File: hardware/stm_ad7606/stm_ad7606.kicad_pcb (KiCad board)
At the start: 2 copper layers, 40.6 x 55.6 mm, 28 parts, among them J1 Conn_01x02_Female, J2 USB_B_Micro, J4 AD7606 Interface, J5 SWD Conn, U1 STM32F103C8Tx, U2 AMS1117-3.3, Y1 8MHz

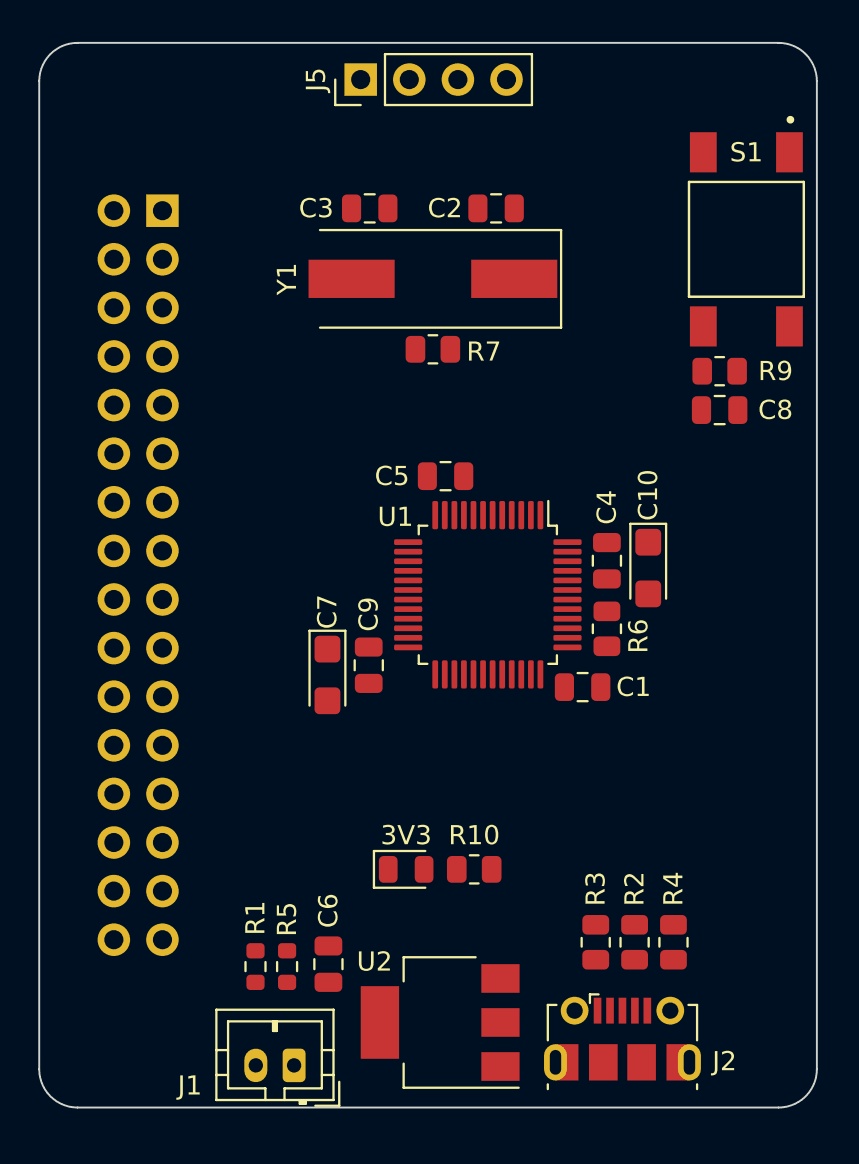
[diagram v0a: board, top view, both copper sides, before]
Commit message: feat[hw]: add interface connection MCU vs 7606
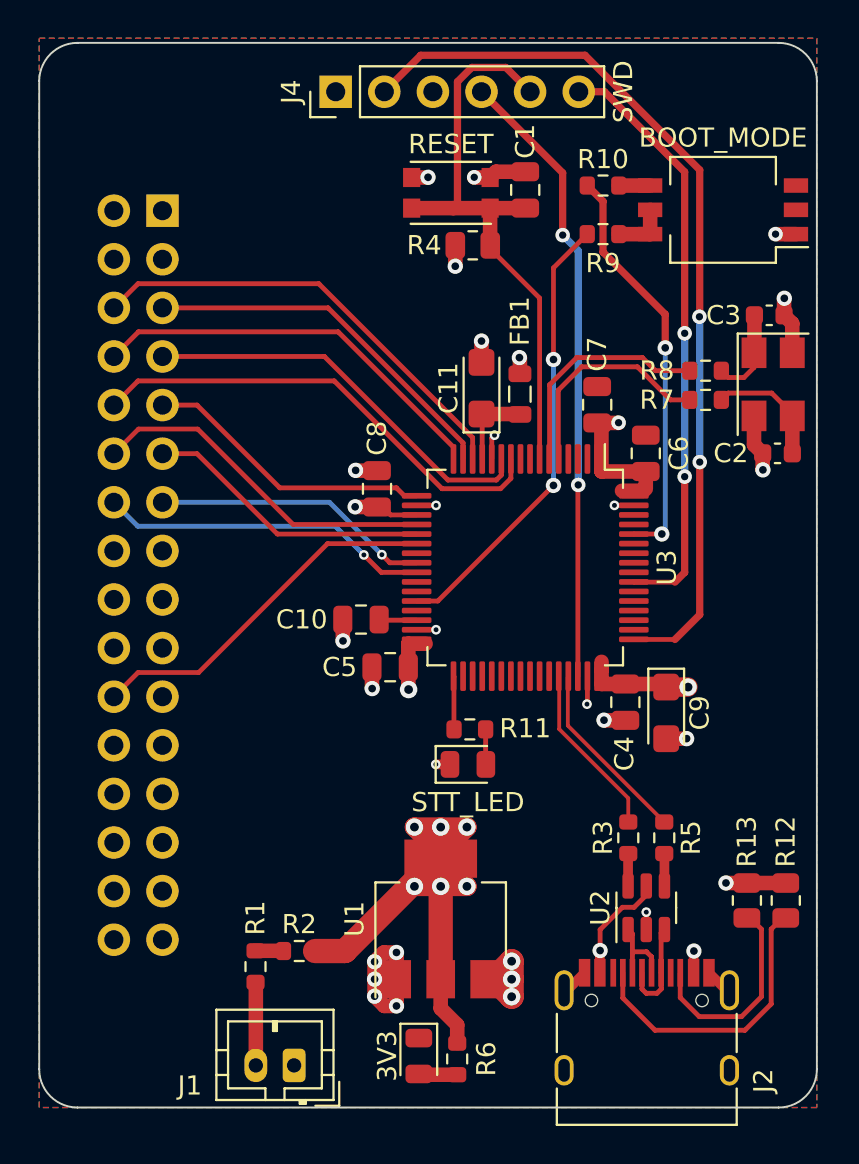
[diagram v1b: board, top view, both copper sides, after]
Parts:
- removed J5: SWD Conn, Connector_PinHeader_2.54mm:PinHeader_1x04_P2.54mm_Vertical
- removed the R2 at (150.2, 113.6)
- added C11: 10u, Capacitor_Tantalum_SMD:CP_EIA-3216-10_Kemet-I, F.Cu at (142.2, 84.6)
- added D2: STT_LED, LED_SMD:LED_0805_2012Metric, F.Cu at (141.5, 104.3)
- added FB1: 600R@100MHz, Inductor_SMD:L_0805_2012Metric, F.Cu at (144.2, 84.9)
- added J4: SWD, Connector_PinHeader_2.54mm:PinHeader_1x06_P2.54mm_Vertical, F.Cu at (134.5, 69.1)
- added R11: 2.49k, Resistor_SMD:R_0603_1608Metric, F.Cu at (141.6, 102.4)
- added R12: 5.1k, Resistor_SMD:R_0805_2012Metric, F.Cu at (158.1, 111.4)
- added R13: 5.1k, Resistor_SMD:R_0805_2012Metric, F.Cu at (156.0, 111.4)
- added R5: 22R, Resistor_SMD:R_0603_1608Metric, F.Cu at (151.7, 108.1)
- added R8: 220R, Resistor_SMD:R_0603_1608Metric, F.Cu at (153.9, 83.7)
- added SW1: BOOT_MODE, Button_Switch_SMD:SW_DIP_SPSTx03_Slide_KingTek_DSHP03TS_W7.62mm_P1.27mm, F.Cu at (154.8, 75.3)
- added U3: STM32F412RETx, Package_QFP:LQFP-64_10x10mm_P0.5mm, F.Cu at (144.5, 94.0)
- C1, C4, C5, C6, C8: value 100nF -> 100n
- C10, C7: value 10uF -> 100n; footprint Capacitor_Tantalum_SMD:CP_EIA-3216-10_Kemet-I -> Capacitor_SMD:C_0805_2012Metric
- C2, C3: value 22pF -> 22p; footprint Capacitor_SMD:C_0805_2012Metric -> Capacitor_SMD:C_0603_1608Metric
- C9: value 100nF -> 10u; footprint Capacitor_SMD:C_0805_2012Metric -> Capacitor_Tantalum_SMD:CP_EIA-3216-10_Kemet-I
- J2: value USB_B_Micro -> USB_C_Receptacle_USB2.0; footprint Connector_USB:USB_Micro-B_Molex-105017-0001 -> Connector_USB:USB_C_Receptacle_HRO_TYPE-C-31-M-12
- R10: value 1k -> 10k; footprint Resistor_SMD:R_0805_2012Metric -> Resistor_SMD:R_0603_1608Metric
- R3: value 20R -> 22R; footprint Resistor_SMD:R_0805_2012Metric -> Resistor_SMD:R_0603_1608Metric
- R4: value 4k7 -> 10k
- R6: value 10k -> 2.49k; footprint Resistor_SMD:R_0805_2012Metric -> Resistor_SMD:R_0603_1608Metric
- R7: value 1M -> 0R; footprint Resistor_SMD:R_0805_2012Metric -> Resistor_SMD:R_0603_1608Metric
- R9: footprint Resistor_SMD:R_0805_2012Metric -> Resistor_SMD:R_0603_1608Metric
- S1: footprint SW1437565-9:SW_4-1437565-9 -> SW-KMR621NGLFS:SW_KMR621NGLFS
- U1: value STM32F103C8Tx -> AMS1117-3.3; footprint Package_QFP:LQFP-48_7x7mm_P0.5mm -> Package_TO_SOT_SMD:SOT-223-3_TabPin2
- U2: value AMS1117-3.3 -> USBLC6-2SC6; footprint Package_TO_SOT_SMD:SOT-223-3_TabPin2 -> Package_TO_SOT_SMD:SOT-23-6
- Y1: footprint Crystal:Crystal_SMD_HC49-SD -> Crystal:Crystal_SMD_5032-4Pin_5.0x3.2mm
- moved R4 37.9 mm to (141.7, 77.1), turned to 0 degrees
- moved R10 36.4 mm to (148.5, 74.0)
- moved C6 31.4 mm to (150.7, 88.0)
- moved C1 26.2 mm to (144.4, 74.2), turned to 90 degrees
- moved R6 23.8 mm to (140.9, 119.7)
- moved C3 21.6 mm to (157.2, 80.8)
- moved C7 20.0 mm to (148.2, 85.5), turned to 90 degrees
- moved C2 19.5 mm to (157.6, 88.0)
- moved Y1 18.6 mm to (157.4, 84.4), turned to -90 degrees
- moved C8 18.4 mm to (136.7, 89.9), turned to 90 degrees
- moved U1 17.1 mm to (140.0, 112.3), turned to 90 degrees
- moved C9 15.7 mm to (151.8, 101.6)
- moved S1 15.6 mm to (140.6, 74.4), turned to 0 degrees
- moved C10 15.3 mm to (135.9, 96.7), turned to 180 degrees
- moved R7 14.5 mm to (153.9, 85.2), turned to 0 degrees
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- renumbered J4 to J3, R5 to R2
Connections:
- C1 pad 1: +3V3 -> nRST
- C10 pad 1: +3V3 -> Net-(C10-Pad1)
- C2 pad 1: /OSCIN -> Net-(C2-Pad1)
- C3 pad 1: /OSCOUT -> Net-(C3-Pad1)
- C8 pad 1: /reset -> +3V3
- J3 pad 15: /AD_DB0 -> unconnected-(J3-Pad15)
- J3 pad 16: /AD_DB1 -> unconnected-(J3-Pad16)
- J3 pad 17: /AD_DB2 -> unconnected-(J3-Pad17)
- J3 pad 18: /AD_DB3 -> unconnected-(J3-Pad18)
- J3 pad 19: /AD_DB4 -> unconnected-(J3-Pad19)
- J3 pad 20: /AD_DB5 -> unconnected-(J3-Pad20)
- J3 pad 21: /AD_DB6 -> unconnected-(J3-Pad21)
- J3 pad 22: /AD_DB7 -> /AD_DOUT_A
- J3 pad 23: /AD_DB8 -> /AD_DOUT_B
- J3 pad 24: /AD_DB9 -> unconnected-(J3-Pad24)
- J3 pad 25: /AD_DB10 -> unconnected-(J3-Pad25)
- J3 pad 26: /AD_DB11 -> unconnected-(J3-Pad26)
- J3 pad 27: /AD_DB12 -> unconnected-(J3-Pad27)
- J3 pad 28: /AD_DB13 -> unconnected-(J3-Pad28)
- J3 pad 29: /AD_DB14 -> unconnected-(J3-Pad29)
- J3 pad 30: /AD_DB15 -> unconnected-(J3-Pad30)
- R10 pad 1: +3V3 -> Net-(R10-Pad1)
- R10 pad 2: Net-(D1-Pad2) -> /MCU_BOOT0
- R3 pad 1: /D- -> Net-(R3-Pad1)
- R3 pad 2: /USBD- -> /MCU_USB_DN
- R4 pad 1: VBUS -> +3V3
- R4 pad 2: /USBD+ -> nRST
- R6 pad 1: GND -> Net-(D1-Pad2)
- R6 pad 2: /BOOT_0 -> +3V3
- R7 pad 1: /OSCIN -> /HSE_OSC_IN
- R7 pad 2: /OSCOUT -> Net-(C2-Pad1)
- R9 pad 1: +3V3 -> Net-(R9-Pad1)
- R9 pad 2: /reset -> /MCU_BOOT1
- U1 pad 1: +BATT -> GND
- U1 pad 2: unconnected-(U1-Pad2) -> +3V3
- U1 pad 3: unconnected-(U1-Pad3) -> VBUS
- U2 pad 1: GND -> /USB_CONN_DN
- U2 pad 2: +3V3 -> GND
- U2 pad 3: VBUS -> /USB_CONN_DP
- Y1 pad 1: /OSCIN -> Net-(C3-Pad1)
- Y1 pad 2: /OSCOUT -> GND
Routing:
- net +3V3: track 0.00 -> 62.4 mm, vias 0 -> 13
- net /SWCLK: track 0.00 -> 47.0 mm, vias 0 -> 2
- net GND: track 0.00 -> 41.4 mm, vias 0 -> 23
- net /SWDIO: track 0.00 -> 32.6 mm, vias 0 -> 2
- net nRST: track 0.00 -> 31.4 mm
- net /SWO: track 0.00 -> 31.1 mm, vias 0 -> 2
- net VBUS: track 0.00 -> 30.8 mm, vias 0 -> 5
- net /AD_RST: track 0.00 -> 24.8 mm
- net /AD_OS1: track 0.00 -> 23.7 mm
- net /MCU_BOOT1: track 0.00 -> 23.5 mm, vias 0 -> 2
- net /MCU_BOOT0: track 0.00 -> 21.4 mm, vias 0 -> 2
- net /AD_ST_A: track 0.00 -> 21.4 mm
- net /AD_OS2: track 0.00 -> 21.3 mm
- net /AD_OS0: track 0.00 -> 19.5 mm
- net /AD_DOUT_A: track 0.00 -> 19.1 mm
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- added copper zone on In2.Cu, net +3V3
- added copper zone on B.Cu, net GND
- added copper zone on F.Cu, net GND
- added copper zone on In1.Cu, net GND
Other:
- copper layers 2 -> 4
